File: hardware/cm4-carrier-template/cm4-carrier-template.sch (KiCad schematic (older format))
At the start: 45 parts, among them J1 USB_C_Receptacle_USB2.0, J2 Micro_SD_Card, J3 Abracon_ARJ-139, J3 Abracon_ARJM11-502, Q1 DMP2066LSN, SW1 BOOT, SW2 GLOBAL_EN, U5 Compute_Module_4_Functional, U6 Expansion_PoE, U6 TPD2EUSB30

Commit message: Finished layout for 40mmx90mm base carrier.
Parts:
- removed J3: Abracon_ARJ-139, jkiv-library:RJ45_Abracon_ARJ136, symbol jkiv-abracon:Abracon_ARJ-139
- removed R13, R14, R15: 0R, Resistor_SMD:R_0603_1608Metric, symbol Device:R_Small_US
- removed R3, R4: 220R, Resistor_SMD:R_0603_1608Metric, symbol Device:R_Small_US
- removed R3, R4: 100R, Resistor_SMD:R_0603_1608Metric, symbol Device:R_Small_US
- removed R5: DNP, Resistor_SMD:R_0603_1608Metric, symbol Device:R_Small_US
- removed U6: Expansion_PoE, jkiv-library:expansion-poe-P2.0mm_SMD, symbol jkiv-expansion:Expansion_PoE
- added JP1: eMMC, jkiv-library:J_Small_NC, symbol Device:Jumper_NC_Small
- added JP2: ~WL_nDisable, jkiv-library:J_Small_NC, symbol Device:Jumper_NC_Small
- added JP3: ~BT_nDisable, jkiv-library:J_Small_NC, symbol Device:Jumper_NC_Small
- added JP4: EEPROM_nWP, jkiv-library:J_Small_NC, symbol Device:Jumper_NC_Small
- added LOGO1: Logo_Open_Hardware_Small, Symbol:OSHW-Symbol_6.7x6mm_Copper, symbol Graphic:Logo_Open_Hardware_Small
- added R3, R4: 220R, Resistor_SMD:R_0603_1608Metric, symbol Device:R_Small_US
- J3: symbol jkiv-abracon:Abracon_ARJM11-502 -> cm4-carrier-template-rescue:Abracon_ARJM11-502-jkiv-abracon
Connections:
- net labels removed: GNDREF, PoE_TAP1, PoE_TAP2, PoE_TAP3, PoE_TAP4, VBUS
- wire segments 162 -> 130
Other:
- note added: "Short = use eMMC\nOpen = use SD card"
- note removed: "Remove shorts to enable features."
- note removed: "Short if eMMC (1.8V)"
- note removed: "TODO CT"

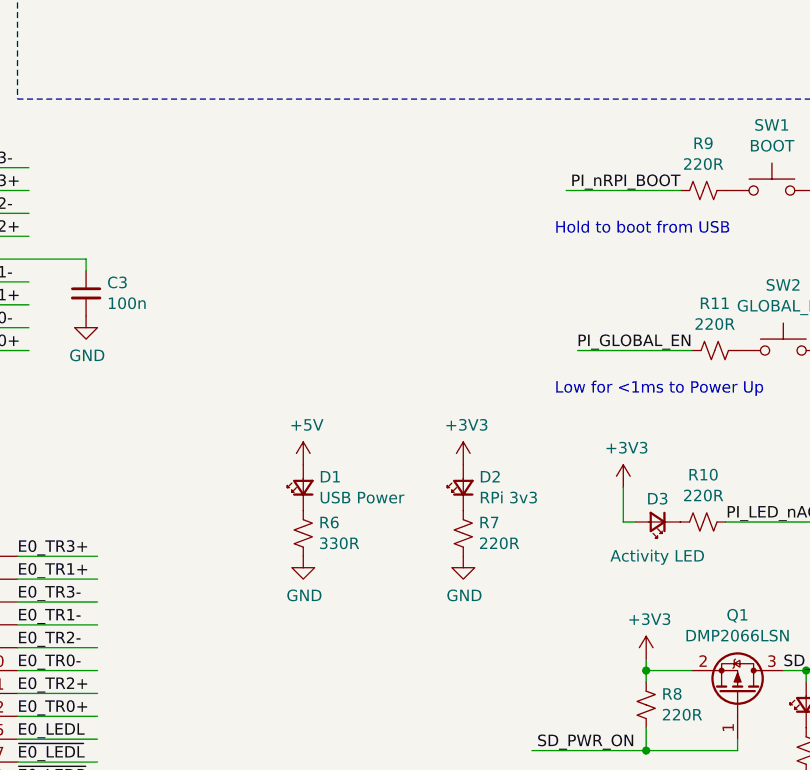
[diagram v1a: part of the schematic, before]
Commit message: Fixed disconnected 'SD enabled' LED.
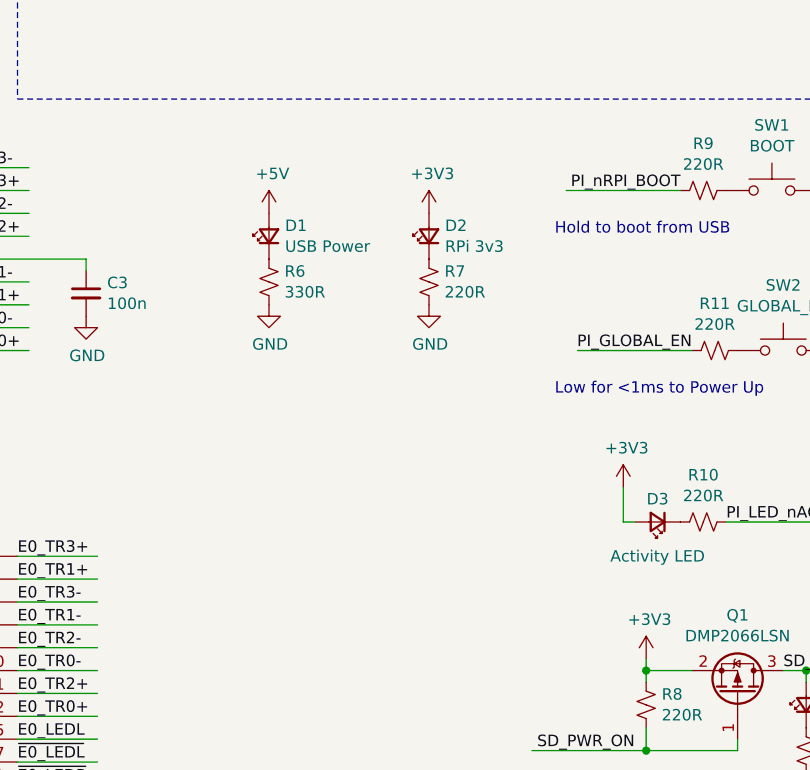
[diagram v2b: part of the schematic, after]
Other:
- moved on the sheet: D1, D2, R6, R7
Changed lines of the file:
@@
 encoding utf-8
 Sheet 1 1
-Title ""
-Date ""
-Rev ""
-Comp ""
-Comment1 ""
+Title "cm4-carrier-template"
+Date "2021-09-17"
+Rev "v1.0a"
+Comp "fourside.io"
+Comment1 "twitch.tv/jkiv"
 Comment2 ""
 Comment3 ""
@@
 L power:GND #PWR0124
 U 1 1 61B0A321
-P 4200 6450
-F 0 "#PWR0124" H 4200 6200 50  0001 C CNN
-F 1 "GND" H 4205 6277 50  0000 C CNN
-F 2 "" H 4200 6450 50  0001 C CNN
-F 3 "" H 4200 6450 50  0001 C CNN
-	1    4200 6450
+P 4050 5350
+F 0 "#PWR0124" H 4050 5100 50  0001 C CNN
+F 1 "GND" H 4055 5177 50  0000 C CNN
+F 2 "" H 4050 5350 50  0001 C CNN
+F 3 "" H 4050 5350 50  0001 C CNN
+	1    4050 5350
 	1    0    0    -1
 $EndComp
@@
 L Device:R_Small_US R6
 U 1 1 61B0B23D
-P 4200 6350
-F 0 "R6" H 4268 6396 50  0000 L CNN
-F 1 "330R" H 4268 6305 50  0000 L CNN
-F 2 "Resistor_SMD:R_0603_1608Metric" H 4200 6350 50  0001 C CNN
-F 3 "~" H 4200 6350 50  0001 C CNN
-	1    4200 6350
+P 4050 5250
+F 0 "R6" H 4118 5296 50  0000 L CNN
+F 1 "330R" H 4118 5205 50  0000 L CNN
+F 2 "Resistor_SMD:R_0603_1608Metric" H 4050 5250 50  0001 C CNN
+F 3 "~" H 4050 5250 50  0001 C CNN
+	1    4050 5250
 	1    0    0    -1
 $EndComp
@@
 L power:+5V #PWR0125
 U 1 1 61B0B247
-P 4200 6050
-F 0 "#PWR0125" H 4200 5900 50  0001 C CNN
-F 1 "+5V" H 4215 6223 50  0000 C CNN
-F 2 "" H 4200 6050 50  0001 C CNN
-F 3 "" H 4200 6050 50  0001 C CNN
-	1    4200 6050
+P 4050 4950
+F 0 "#PWR0125" H 4050 4800 50  0001 C CNN
+F 1 "+5V" H 4065 5123 50  0000 C CNN
+F 2 "" H 4050 4950 50  0001 C CNN
+F 3 "" H 4050 4950 50  0001 C CNN
+	1    4050 4950
 	1    0    0    -1
 $EndComp
@@
 L Device:LED_Small D1
 U 1 1 61B0B251
-P 4200 6150
-F 0 "D1" V 4246 6080 50  0000 R CNN
-F 1 "USB Power" V 4155 6080 50  0000 R CNN
-F 2 "LED_SMD:LED_0603_1608Metric" V 4200 6150 50  0001 C CNN
-F 3 "~" V 4200 6150 50  0001 C CNN
-	1    4200 6150
+P 4050 5050
+F 0 "D1" V 4096 4980 50  0000 R CNN
+F 1 "USB Power" V 4005 4980 50  0000 R CNN
+F 2 "LED_SMD:LED_0603_1608Metric" V 4050 5050 50  0001 C CNN
+F 3 "~" V 4050 5050 50  0001 C CNN
+	1    4050 5050
 	0    -1   -1   0
 $EndComp
@@
 L power:GND #PWR0126
 U 1 1 61B1A939
-P 4900 6450
-F 0 "#PWR0126" H 4900 6200 50  0001 C CNN
-F 1 "GND" H 4905 6277 50  0000 C CNN
-F 2 "" H 4900 6450 50  0001 C CNN
-F 3 "" H 4900 6450 50  0001 C CNN
-	1    4900 6450
+P 4750 5350
+F 0 "#PWR0126" H 4750 5100 50  0001 C CNN
+F 1 "GND" H 4755 5177 50  0000 C CNN
+F 2 "" H 4750 5350 50  0001 C CNN
+F 3 "" H 4750 5350 50  0001 C CNN
+	1    4750 5350
 	1    0    0    -1
 $EndComp
@@
 L Device:R_Small_US R7
 U 1 1 61B1B89B
-P 4900 6350
-F 0 "R7" H 4968 6396 50  0000 L CNN
-F 1 "220R" H 4968 6305 50  0000 L CNN
-F 2 "Resistor_SMD:R_0603_1608Metric" H 4900 6350 50  0001 C CNN
-F 3 "~" H 4900 6350 50  0001 C CNN
-	1    4900 6350
+P 4750 5250
+F 0 "R7" H 4818 5296 50  0000 L CNN
+F 1 "220R" H 4818 5205 50  0000 L CNN
+F 2 "Resistor_SMD:R_0603_1608Metric" H 4750 5250 50  0001 C CNN
+F 3 "~" H 4750 5250 50  0001 C CNN
+	1    4750 5250
 	1    0    0    -1
 $EndComp
@@
 L Device:LED_Small D2
 U 1 1 61B1B8AF
-P 4900 6150
-F 0 "D2" V 4946 6080 50  0000 R CNN
-F 1 "RPi 3v3" V 4855 6080 50  0000 R CNN
-F 2 "LED_SMD:LED_0603_1608Metric" V 4900 6150 50  0001 C CNN
-F 3 "~" V 4900 6150 50  0001 C CNN
-	1    4900 6150
+P 4750 5050
+F 0 "D2" V 4796 4980 50  0000 R CNN
+F 1 "RPi 3v3" V 4705 4980 50  0000 R CNN
+F 2 "LED_SMD:LED_0603_1608Metric" V 4750 5050 50  0001 C CNN
+F 3 "~" V 4750 5050 50  0001 C CNN
+	1    4750 5050
 	0    -1   -1   0
 $EndComp
@@
 L power:+3V3 #PWR0116
 U 1 1 61C065BC
-P 4900 6050
-F 0 "#PWR0116" H 4900 5900 50  0001 C CNN
-F 1 "+3V3" H 4915 6223 50  0000 C CNN
-F 2 "" H 4900 6050 50  0001 C CNN
-F 3 "" H 4900 6050 50  0001 C CNN
-	1    4900 6050
-	1    0    0    -1
-$EndComp
+P 4750 4950
+F 0 "#PWR0116" H 4750 4800 50  0001 C CNN
+F 1 "+3V3" H 4765 5123 50  0000 C CNN
+F 2 "" H 4750 4950 50  0001 C CNN
+F 3 "" H 4750 4950 50  0001 C CNN
+	1    4750 4950
+	1    0    0    -1
+$EndComp

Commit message: Ok. Symbol libraries /should/ be fixed... 🤞
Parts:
- J3: symbol cm4-carrier-template-rescue:Abracon_ARJM11-502-jkiv-abracon -> jkiv-abracon:Abracon_ARJM11-502
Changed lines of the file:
@@
 	2650 4950 3000 4950
 $Comp
-L cm4-carrier-template-rescue:Abracon_ARJM11-502-jkiv-abracon J3
+L jkiv-abracon:Abracon_ARJM11-502 J3
 U 1 1 61426389
 P 2150 5150

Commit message: Updated USB connector to what is available. Generated gerbers, HTMLBOM.
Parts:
- J1: footprint Connector_USB:USB_C_Receptacle_Palconn_UTC16-G -> jkiv-library:USB_C_Receptacle_GCT-USB4105
- U5: Digi-Key_PN (none) -> DF40HC(3.0)-100DS-0.4V(51-ND; MPN (none) -> DF40HC(3.0)-100DS-0.4V(51
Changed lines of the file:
@@
 F 2 "RPi_Compute_Module_4:Raspberry-Pi-4-Compute-Module" H 7200 1650 60  0001 L CNN
 F 3 "" H 7200 1450 60  0001 L CNN
+F 4 "DF40HC(3.0)-100DS-0.4V(51-ND" H 7000 1600 50  0001 C CNN "Digi-Key_PN"
+F 5 "DF40HC(3.0)-100DS-0.4V(51" H 7000 1600 50  0001 C CNN "MPN"
 	10   7000 1600
 	1    0    0    -1
@@
 F 0 "J1" H 1107 2667 50  0000 C CNN
 F 1 "USB_C_Receptacle_USB2.0" H 1107 2576 50  0000 C CNN
-F 2 "Connector_USB:USB_C_Receptacle_Palconn_UTC16-G" H 1150 1800 50  0001 C CNN
+F 2 "jkiv-library:USB_C_Receptacle_GCT-USB4105" H 1150 1800 50  0001 C CNN
 F 3 "https://www.usb.org/sites/default/files/documents/usb_type-c.zip" H 1150 1800 50  0001 C CNN
 	1    1000 1800

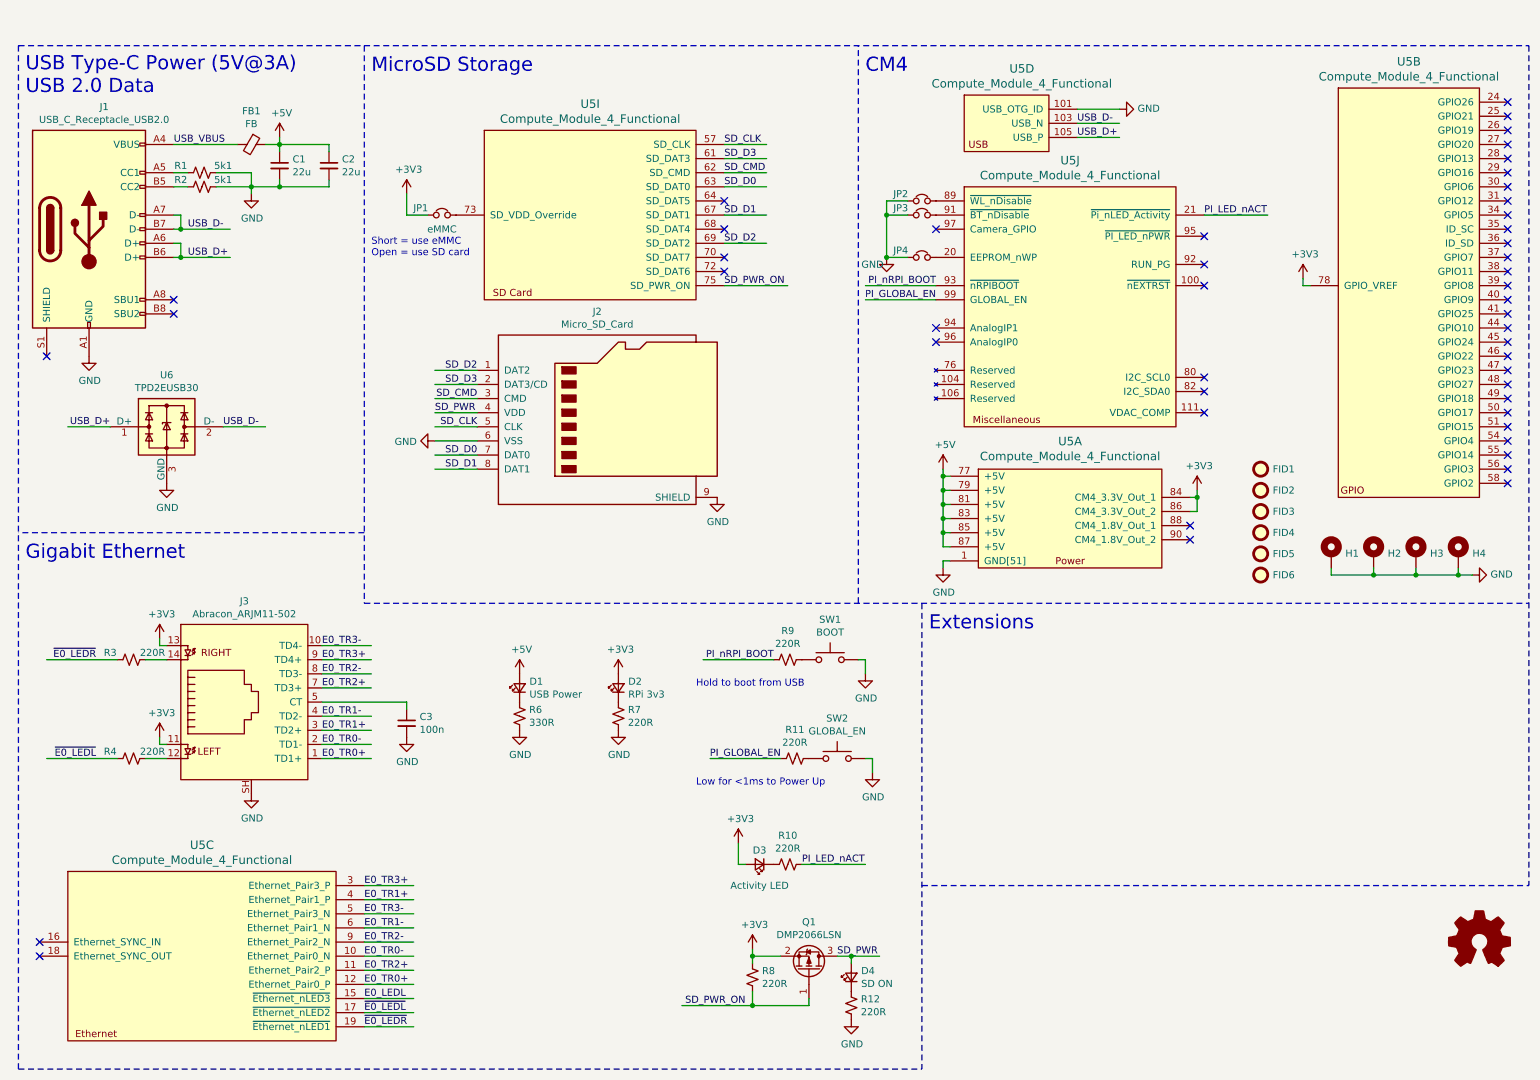
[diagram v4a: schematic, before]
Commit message: Reworked cm4-carrier-template using latest cm4-carrier-net as base.
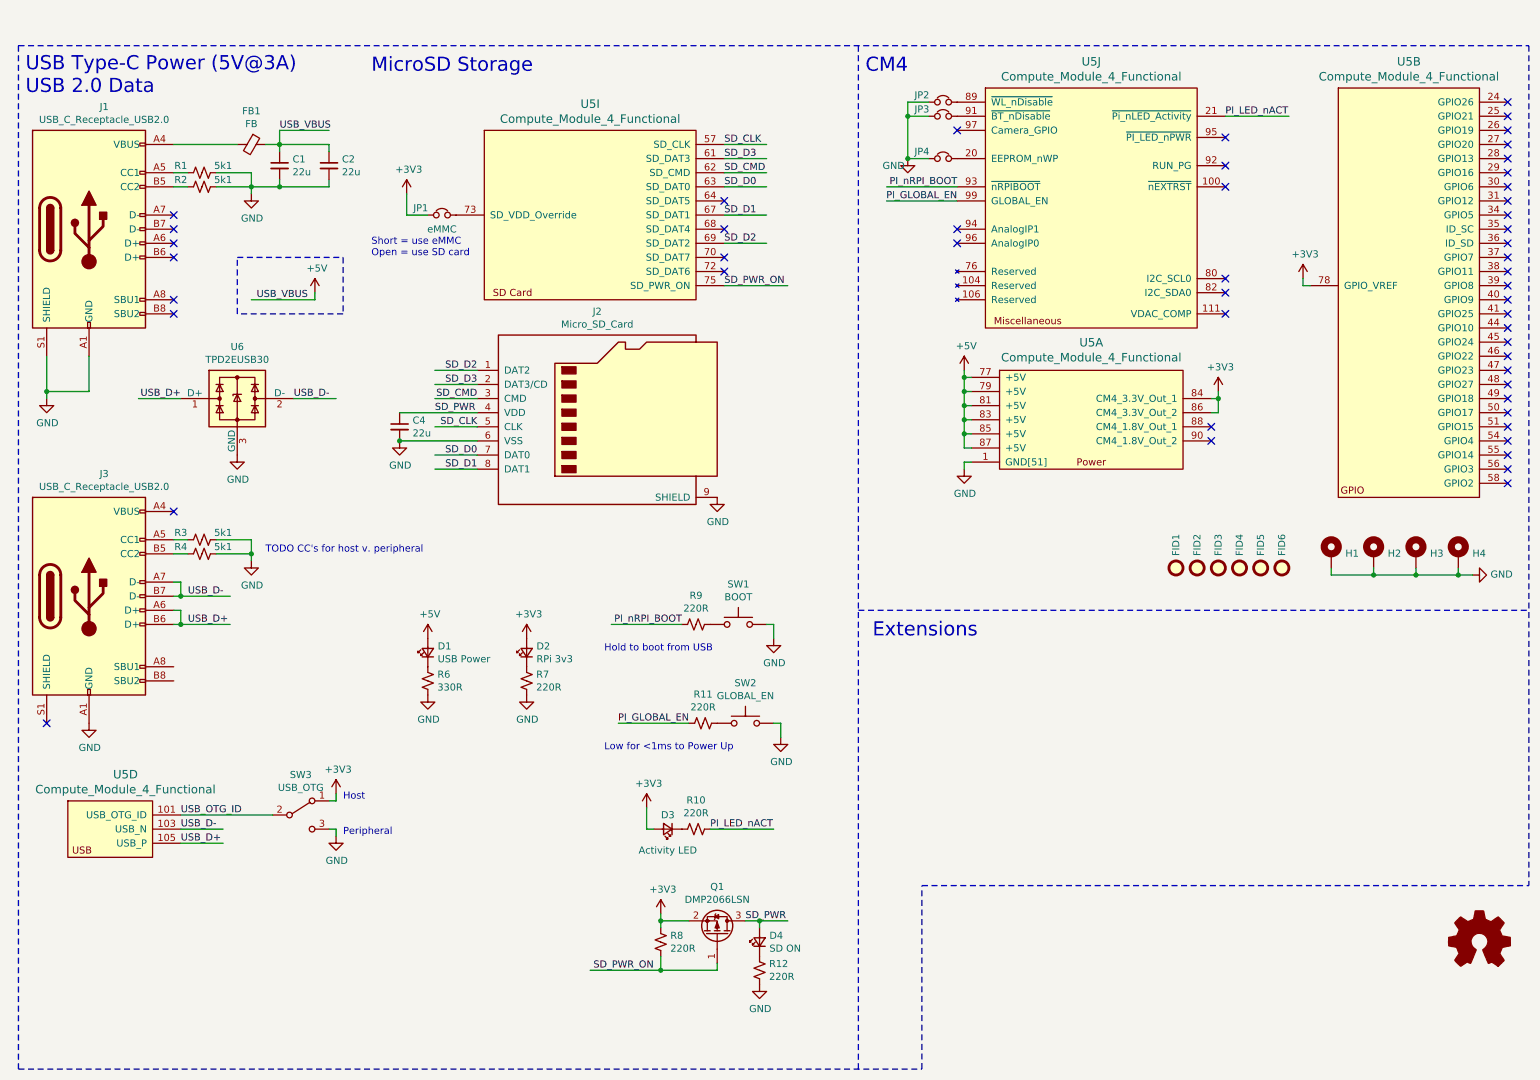
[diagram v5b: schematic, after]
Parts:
- removed C3: 100n, Capacitor_SMD:C_0805_2012Metric, symbol Device:C_Small
- removed J3: Abracon_ARJM11-502, jkiv-library:RJ45_Abracon_ARJM11, symbol jkiv-abracon:Abracon_ARJM11-502
- removed unit 3 of U5
- added C4: 22u, Capacitor_SMD:C_0805_2012Metric, symbol Device:C_Small
- added J3: USB_C_Receptacle_USB2.0, jkiv-library:USB_C_Receptacle_GCT-USB4105, symbol Connector:USB_C_Receptacle_USB2.0
- added SW3: USB_OTG, Button_Switch_SMD:SW_SPDT_CK-JS102011SAQN, symbol Switch:SW_SPDT
- R3, R4: value 220R -> 5k1
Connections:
- net labels added: USB_OTG_ID
- net labels removed: E0_LEDL, E0_TR0+, E0_TR0-, E0_TR1+, E0_TR1-, E0_TR2+, E0_TR2-, E0_TR3+, E0_TR3-, ~E0_LEDL, ~E0_LEDR
- wire segments 130 -> 118
- no-connect marks 48 -> 51
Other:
- note added: "Host"
- note added: "Peripheral"
- note added: "TODO CC's for host v. peripheral"
- note removed: "Gigabit Ethernet"
- moved on the sheet: D1, D2, D3, D4, FID1, FID2, FID3, FID4, FID5, FID6, JP2, JP3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
